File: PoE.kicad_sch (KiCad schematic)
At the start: 78 parts, among them J13 Conn_01x03_Male, Q2 BSZ440N10NS3GATMA1, T1 PA2467NL, U23 TPS23734, U24 TCMT1107

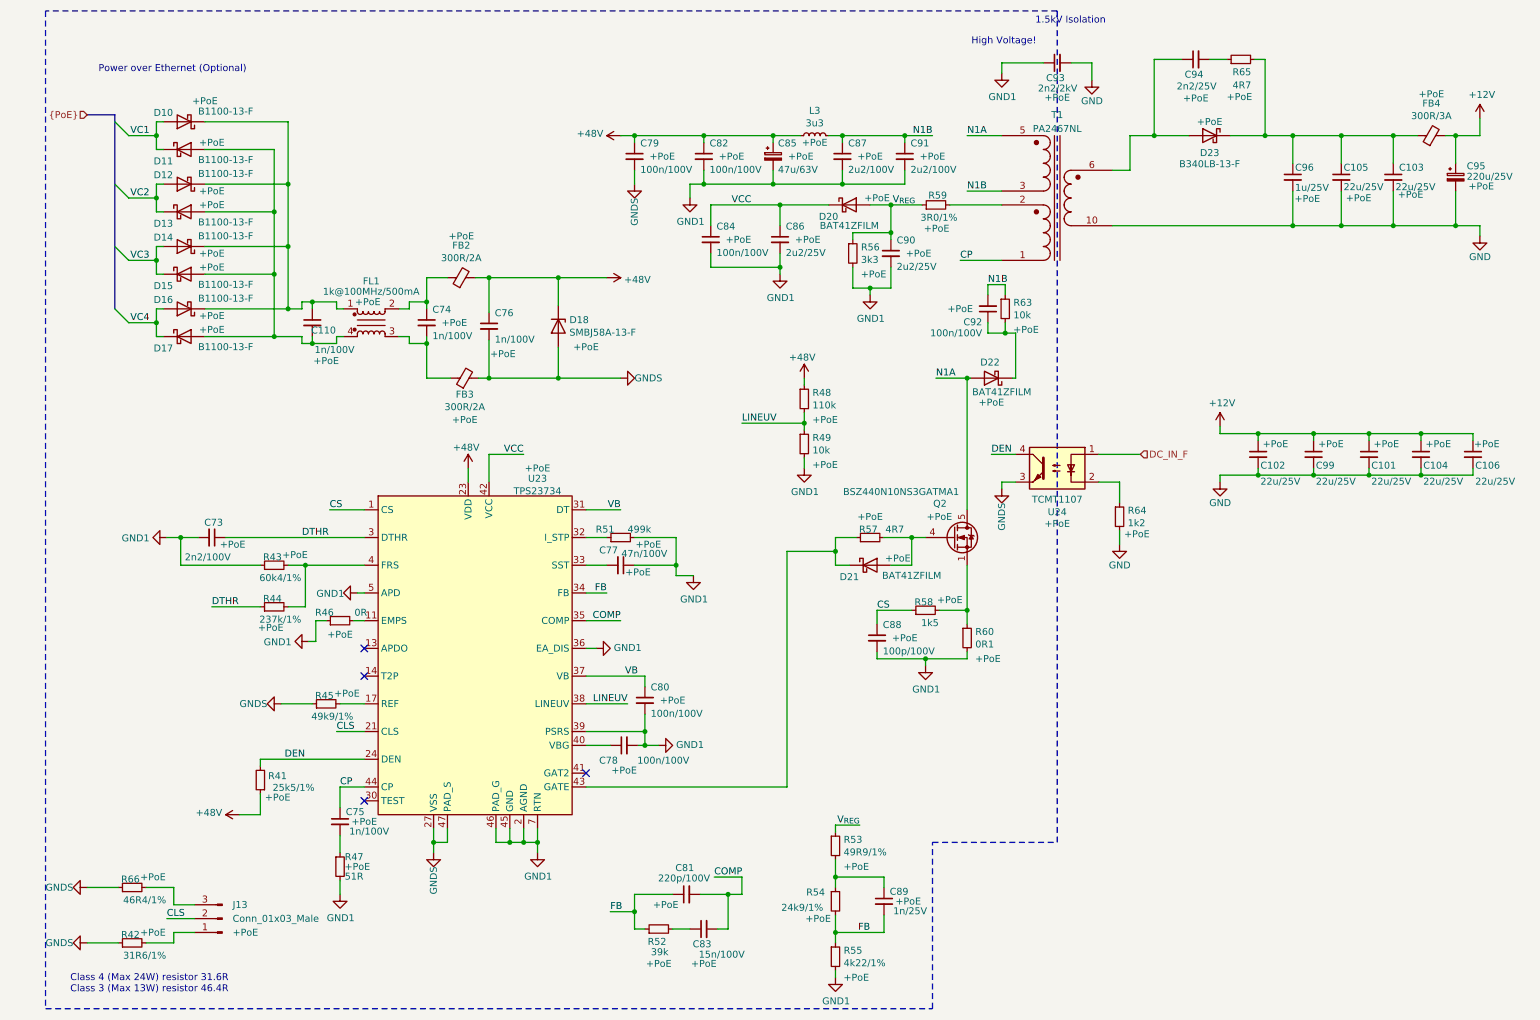
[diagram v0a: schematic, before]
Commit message: Mark Transformer Pulse PA2467NL as PoE only
Set Config +PoE to make sure that Pulse is only assembled in PoE BOM.

Signed-off-by: Stefan Agner <stefan@agner.ch>
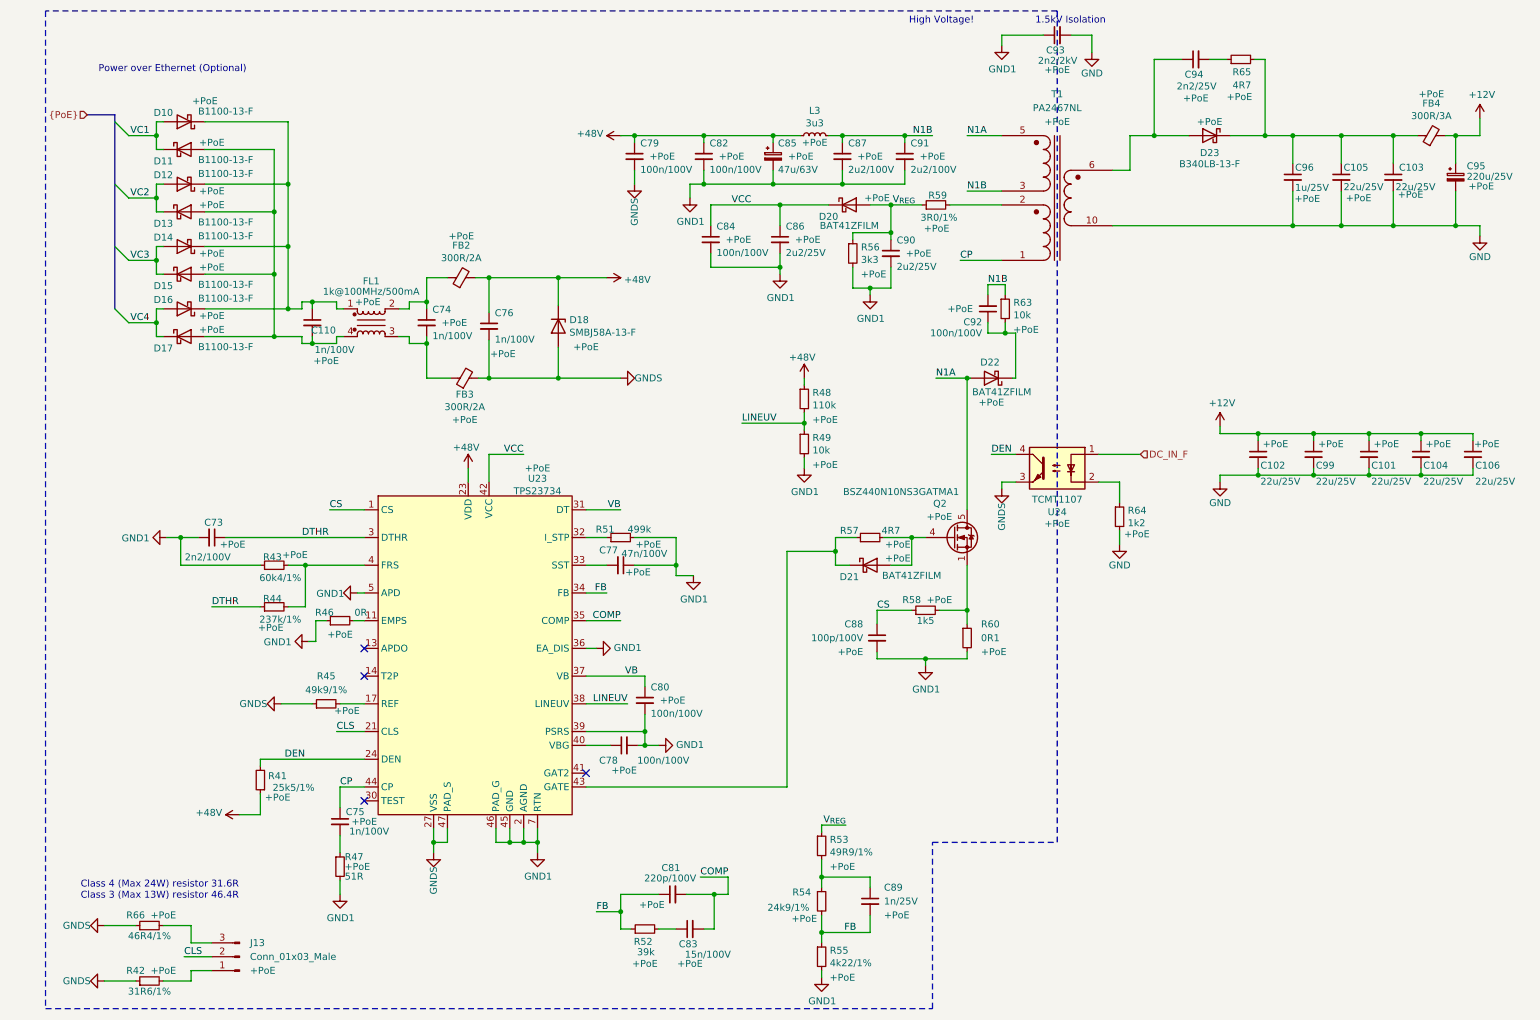
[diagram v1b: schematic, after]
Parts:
- T1: Config (none) -> +PoE
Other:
- moved on the sheet: C81, C83, C89, C93, J13, R42, R52, R53, R54, R55, R66

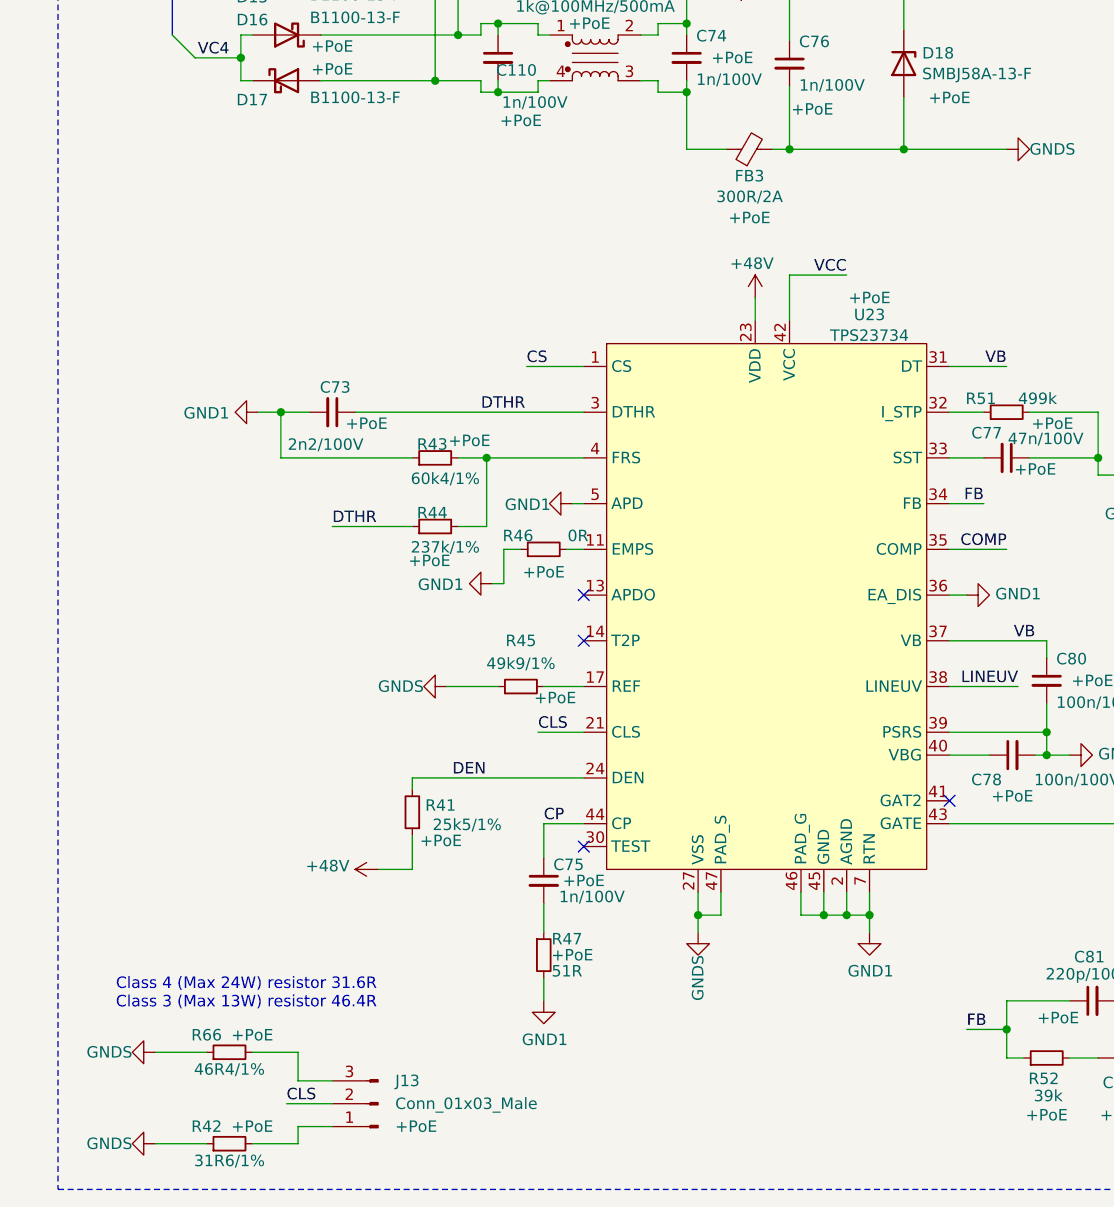
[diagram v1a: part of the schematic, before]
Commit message: Begin replacing TPS23734 with MPS MP8008
Signed-off-by: Stefan Agner <stefan@agner.ch>
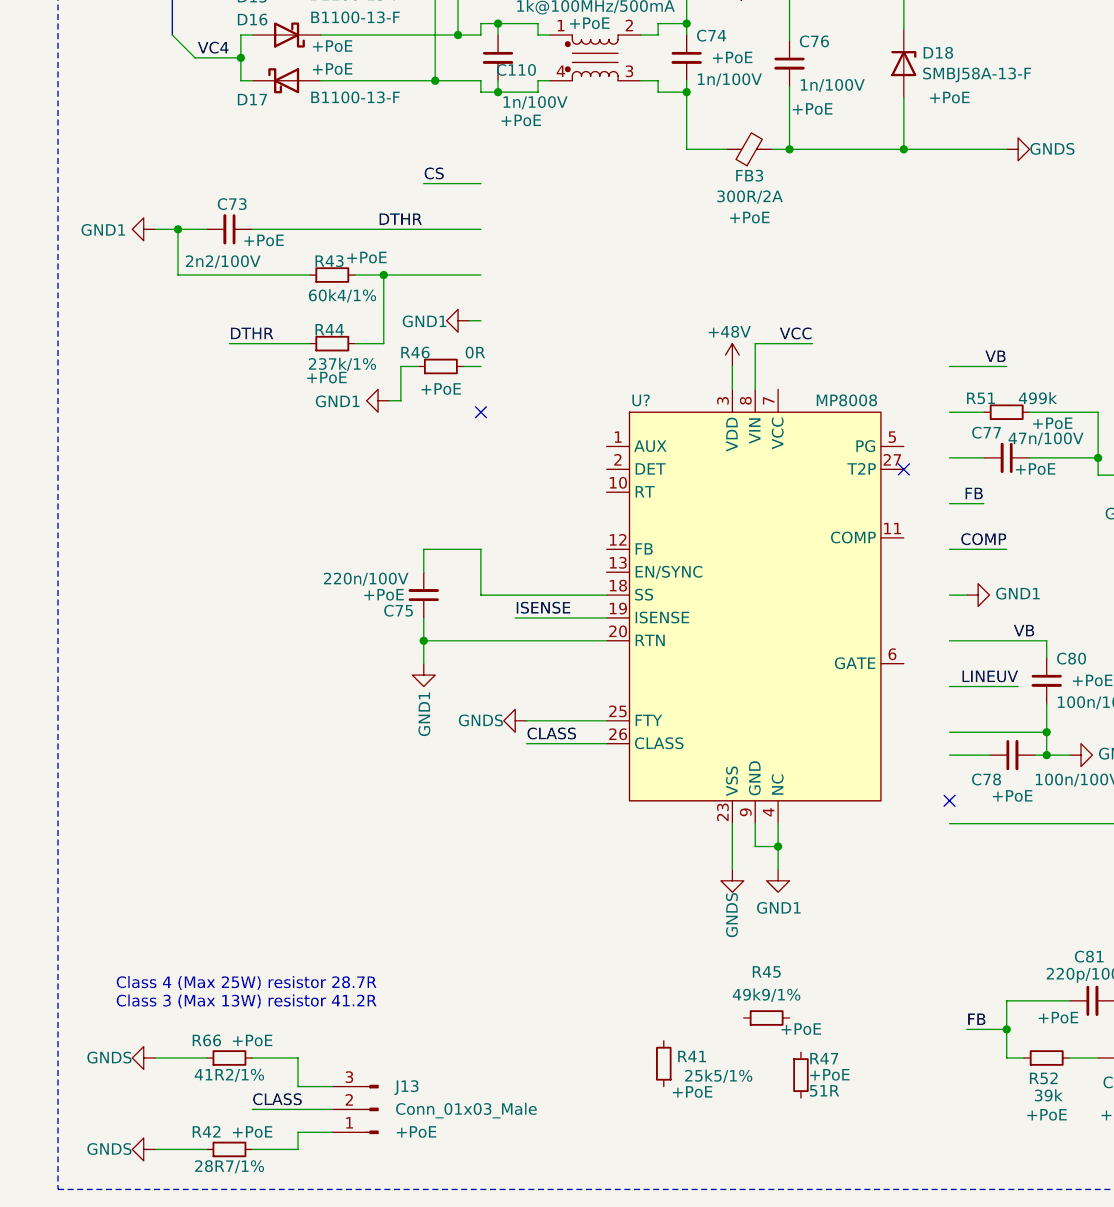
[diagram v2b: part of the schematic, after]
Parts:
- removed U23: TPS23734, Amber:Texas_VQFN-47-2EP_5x7mm_P0.4mm_ThermalVias, symbol Amber:TPS23734
- added U?: MP8008, Package_DFN_QFN:QFN-28-1EP_4x5mm_P0.5mm_EP2.65x3.65mm_ThermalVias, symbol Amber:MP8008
- C75: value 1n/100V -> 220n/100V
- R42: value 31R6/1% -> 28R7/1%
- R66: value 46R4/1% -> 41R2/1%
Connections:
- net +48V: now also U?.3 (VDD); no longer R41.1
- net CP: no longer C75.1
- net DEN: no longer R41.2
- net GND1: now also C75.1, U?.14 (NC), U?.15 (NC), U?.16 (NC), U?.17 (NC), U?.20 (RTN), U?.21 (RTN), U?.22 (NC), U?.28 (NC), U?.4 (NC), U?.9 (GND); no longer R47.2
- net GNDS: now also U?.23 (VSS), U?.24 (VSS), U?.25 (FTY); no longer R45.1
- net VCC: now also U?.8 (VIN)
- net at C75.2: now also U?.18 (SS); no longer R47.1
- net CLS renamed CLASS
- net CLASS: now also U?.26 (CLASS)
- new net ISENSE: U?.19 (ISENSE)
- no-connect marks 4 -> 3
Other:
- note added: "Class 4 (Max 25W) resistor 28.7R Class 3 (Max 13W) resistor 41.2R"
- note removed: "Class 4 (Max 24W) resistor 31.6R Class 3 (Max 13W) resistor 46.4R"
- moved on the sheet: C73, C75, J13, R41, R42, R43, R44, R45, R46, R47, R66
